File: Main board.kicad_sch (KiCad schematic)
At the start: 101 parts, among them CN1 PA001-4P, CN2 PA001-4P, J1 Conn_ARM_SWD_TagConnect_TC203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, J2 Conn_01x03_Pin, J3 Conn_01x03_Pin, J5 Connector, USB-TYPE-C-16P, J6 436500201, J7 Conn_01x04_Pin, J8 Conn_01x04_Pin, Q1 SI7232DN-T1-GE3, Q2 SI7232DN-T1-GE3, SW1 SKRKAEE020, SW2 SKRKAEE020, U1 STM32U575VGTx, U10 TLV75733PDBV, U11 NRVB120VLSFT1G, U12 NRVB120VLSFT1G, U2 TPS62901RPJR, U7 SN74AHCT125DR, X1 1XXD32000MBA, Y1 ECS-327TXO-33-TR

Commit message: fix and back to basic
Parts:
- removed CN1, CN2: PA001-4P, EASYEDA:CONN-TH_4P-P5.08_PA001-4P, symbol EasyEDA:PA001-4P
- removed J2, J3: Conn_01x03_Pin, Connector_PinHeader_2.54mm:PinHeader_1x03_P2.54mm_Horizontal, symbol Connector:Conn_01x03_Pin
- added CN1, CN2: PA001-6P, Mainboard_local:CONN-TH_6P-P5.00_PA001-6P, symbol Mainboard_local:PA001-6P
- added J2: Conn_01x02_Pin, Connector_PinHeader_2.54mm:PinHeader_1x02_P2.54mm_Vertical, symbol Connector:Conn_01x02_Pin
- added J3: Conn_01x02_Pin, Connector_AMASS:AMASS_XT30PW-F_1x02_P2.50mm_Horizontal, symbol Connector:Conn_01x02_Pin
- added SW3, SW4: SW_SPDT, EasyEDA:SW-TH_3P-L8.8-W3.9-P2.50_SS12D00G3, symbol Switch:SW_SPDT
- C1, C25, C26, C35, C36: footprint PCM_JLCPCB:C_0603 -> PCM_JLCPCB:C_0402; LCSC C96446 -> C15525; Price 0.007USD -> 0.009USD; Stock 2048985 -> 3940889; Voltage Rated 25V -> 6.3V
- C10, C11, C12, C15, C2, C3, C30, C4, C5, C6, C7, C8, C9: Stock 12931403 -> 20208285
- C13, C14: Stock 4952869 -> 7021828
- C27, C31: Price 0.017USD -> 0.021USD; Stock 2472302 -> 3388297
- C28: footprint PCM_JLCPCB:C_0805 -> PCM_JLCPCB:C_0603; LCSC C380338 -> C59461; Price 0.010USD -> 0.012USD; Stock 1921885 -> 5081183; Voltage Rated 10V -> 6.3V
- C29: Stock 2965057 -> 4779042
- C32, C37: Stock 52215439 -> 70324515
- C34: footprint PCM_JLCPCB:C_0805 -> PCM_JLCPCB:C_0402; LCSC C76639 -> C23733; Stock 1920914 -> 4366811
- J7: value Conn_01x04_Pin -> Conn_01x02_Pin; footprint Connector_JST:JST_XH_B4B-XH-A_1x04_P2.50mm_Vertical -> Connector_JST:JST_XH_B2B-XH-A_1x02_P2.50mm_Vertical; symbol Connector:Conn_01x04_Pin -> Connector:Conn_01x02_Pin
- R1, R10, R11, R12, R13, R19, R9: Attrition Qty 0 -> 10; LCSC C25744 (OUT OF STOCK) -> C25744; Minimum Qty 5 -> 20; Stock 10588972 -> 24372091
- R15, R16, R3, R4: Stock 1915978 -> 7466061
- R2, R32, R33, R34: Stock 858002 -> 967219
- R20: Stock 4940693 -> 5907585
- R21, R29, R39, R44: Stock 591787 -> 1007760
- R22, R23: Stock 2252456 -> 3534773
- R24: LCSC - -> C22764; Manufacturer Panasonic -> UNI-ROYAL(Uniroyal Elec); Part ERJ-P03F7682V -> 0603WAF1101T5E; Power(Watts) 200mW -> 100mW; Resistance 76.8kΩ -> 1.1kΩ; Stock 71476 -> 156127
- R25: LCSC - -> C22764; Manufacturer Panasonic -> UNI-ROYAL(Uniroyal Elec); Part ERJ-S03F2612V -> 0603WAF1101T5E; Resistance 26.1kΩ -> 1.1kΩ; Stock 71476 -> 156127
- R26: Stock 28829731 -> 51181774
- R27: Stock 1745486 -> 1792808
- R28: Stock 230104 -> 203255
- R35, R36, R37, R38: Stock 8207005 -> 13226393
- R40, R41, R42, R43: Stock 663196 -> 859014
- R5, R8: Stock 480893 -> 771013
- R7: LCSC C25741 (OUT OF STOCK) -> C25741; Stock 4653113 -> 6969783
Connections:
- net GNDA is gone; now on net GND: H1.1, H2.1, H3.1, H4.1
- net +3V3: no longer J7.1 (Pin_1)
- net GND: now also CN1.4, CN2.4, J2.2 (Pin_2), J3.2 (Pin_2); no longer J7.2 (Pin_2)
- net PYRO+: now also CN1.1, CN2.1, SW3.3 (C), SW4.3 (C)
- net SERVO1: now also CN1.5
- net SERVO2: now also CN2.5
- net USART1_RX: now also J7.2 (Pin_2); no longer J7.4 (Pin_4)
- net USART1_TX: now also J7.1 (Pin_1); no longer J7.3 (Pin_3)
- net VBAT+: now also J3.1 (Pin_1)
- net at Q1.5 (D2), Q1.6 (D2), R41.2: now also CN1.6
- net at Q1.7 (D1), Q1.8 (D1), R40.2: now also CN1.2
- net at Q2.5 (D2), Q2.6 (D2), R42.2: now also CN2.6
- net at Q2.7 (D1), Q2.8 (D1), R43.2: now also CN2.2
- new net: CN2.3, SW4.2 (B)
- new net: CN1.3, SW3.2 (B)
- new net BEC+: J2.1 (Pin_1), SW3.1 (A), SW4.1 (A)
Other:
- note added: "A0 · Mounting Holes"
- note added: "A1 · Battery Input & Protection"
- note added: "A1.2 · Battery Voltage Sense (ADC divider)"
- note added: "A2 · 5V Buck (TPS62901RPJR set for vset mode)"
- note added: "A3 · 3.3V LDO (TLV75733)"
- note added: "A4 · BEC interface (servo supply rail)"
- note added: "A5 · Actuation"
- note added: "B1 · MCU Core - STM32U575"
- note added: "B1 · MCU Decoupling"
- note added: "B2 · Clock - 32 MHz HSE (X1)"
- note added: "B2 · Clock - 32.768 kHz LSE (Y1)"
- note added: "B4 · microSD Storage"
- note added: "B5 · Actuation - Servo Level Shift"
- note added: "C1 · USB Interface + ESD diodes"
- note added: "C2 · Comms - USART1 (Companion)"
- note added: "C2 · Comms - USART3 (Telemetry)"
- note added: "D1 · BOOT0 Button"
- note added: "D1 · Reset Button"
- note added: "D1 · Status LEDs"
- note added: "D2 · SWD Debug (TagConnect)"
- note removed: "3.3V LDO"
- note removed: "5V Buck (TPS62901RPJR set for vset mode)"
- note removed: "BOOT0 switch"
- note removed: "Battery Connector"
- note removed: "Companion USART1"
- note removed: "Debugging"
- note removed: "Divider circuit for ADC"
- note removed: "LSE 32.7680 kHz"
- note removed: "MCU Power and Decoupling"
- note removed: "Manual reset"
- note removed: "PWM Level Shifting"
- note removed: "Pyrotechnique channels"
- note removed: "SD Card slot"
- note removed: "STM32U5"
- note removed: "TCXO"
- note removed: "Transmission USART3"
- note removed: "USB + ESD diodes"
- company: Chulalongkorn University High Altitude Research (CUHAR) -> (none)
- title: CURFA-V SRAD Flight Computer -> CANSR-I SRAD Flight Computer
- moved on the sheet: C1, C10, C11, C12, C13, C14, C15, C2, C25, C26, C27, C28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

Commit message: fix + start leyout
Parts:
- C30, D2, R27, R28: now left out of the parts list
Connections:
- net BEC+: now also J2.2 (Pin_2); no longer J2.1 (Pin_1)
- net GND: now also J2.1 (Pin_1), J3.1 (Pin_1), J6.1; no longer J2.2 (Pin_2), J3.2 (Pin_2), J6.2
- net PYRO+: now also J6.2; no longer J6.1
- net VBAT+: now also J3.2 (Pin_2); no longer J3.1 (Pin_1)
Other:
- moved on the sheet: C31, C32, D3, J3, J6, JP1

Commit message: Update Main board.kicad_sch
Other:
- title: CANSR-I SRAD Flight Computer -> COMSR-I
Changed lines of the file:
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@@
 	(paper "A3")
 	(title_block
-		(title "CANSR-I SRAD Flight Computer")
+		(title "COMSR-I")
 		(rev "1.1.31")
 	)

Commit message: koiiin
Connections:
- net at SW4.2 (B): now also CN2.6; no longer CN2.3
- net at SW3.2 (B): now also CN1.6; no longer CN1.3
- net at Q1.5 (D2), Q1.6 (D2), R41.2: now also CN1.3; no longer CN1.6
- net at Q2.5 (D2), Q2.6 (D2), R42.2: now also CN2.3; no longer CN2.6
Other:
- moved on the sheet: CN1, CN2

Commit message: 80%layout
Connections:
- net FIRE_C: now also U1.7 (PC13); no longer U1.9 (PC15)
- net FIRE_D: now also U1.9 (PC15); no longer U1.7 (PC13)
- net PWM1: now also U7.5 (2A); no longer U7.2 (1A)
- net PWM2: now also U7.2 (1A); no longer U7.5 (2A)
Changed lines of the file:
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@@
 	(wire
 		(pts
+			(xy 273.05 165.1) (xy 274.32 165.1)
+		)
+		(stroke
+			(width 0)
+			(type default)
+		)
+	)
+	(wire
+		(pts
 			(xy 153.67 229.87) (xy 148.59 229.87)
 		)
@@
 	(wire
 		(pts
+			(xy 273.05 170.18) (xy 274.32 170.18)
+		)
+		(stroke
+			(width 0)
+			(type default)
+		)
+	)
+	(wire
+		(pts
 			(xy 19.05 36.83) (xy 26.67 36.83)
 		)
@@
 	(wire
 		(pts
+			(xy 120.65 125.73) (xy 128.27 125.73)
+		)
+		(stroke
+			(width 0)
+			(type default)
+		)
+	)
+	(wire
+		(pts
 			(xy 273.05 99.06) (xy 274.32 99.06)
 		)
@@
 	(wire
 		(pts
-			(xy 339.09 86.36) (xy 349.25 86.36)
+			(xy 120.65 133.35) (xy 128.27 133.35)
 		)
 		(stroke
@@
 	(wire
 		(pts
-			(xy 40.64 139.7) (xy 59.69 139.7)
+			(xy 339.09 86.36) (xy 349.25 86.36)
 		)
 		(stroke
@@
 	(wire
 		(pts
-			(xy 44.45 182.88) (xy 46.99 182.88)
+			(xy 40.64 139.7) (xy 59.69 139.7)
 		)
 		(stroke
@@
 	(wire
 		(pts
-			(xy 252.73 33.02) (xy 255.27 33.02)
+			(xy 44.45 182.88) (xy 46.99 182.88)
 		)
 		(stroke
@@
 	(wire
 		(pts
-			(xy 40.64 129.54) (xy 49.53 129.54)
+			(xy 252.73 33.02) (xy 255.27 33.02)
 		)
 		(stroke
@@
 	(wire
 		(pts
-			(xy 45.72 36.83) (xy 26.67 36.83)
+			(xy 40.64 129.54) (xy 49.53 129.54)
 		)
 		(stroke
@@
 	(wire
 		(pts
-			(xy 26.67 39.37) (xy 36.83 39.37)
+			(xy 45.72 36.83) (xy 26.67 36.83)
 		)
 		(stroke
@@
 	(wire
 		(pts
-			(xy 116.84 125.73) (xy 128.27 125.73)
+			(xy 26.67 39.37) (xy 36.83 39.37)
 		)
 		(stroke
@@
 	(wire
 		(pts
-			(xy 116.84 133.35) (xy 128.27 133.35)
-		)
-		(stroke
-			(width 0)
-			(type default)
-		)
-	)
-	(wire
-		(pts
 			(xy 330.2 113.03) (xy 330.2 111.76)
 		)
@@
 	(global_label "FIRE_D"
 		(shape output)
-		(at 273.05 165.1 0)
+		(at 274.32 170.18 0)
 		(fields_autoplaced yes)
 		(effects
@@
 		)
 		(property "Intersheetrefs" "${INTERSHEET_REFS}"
-			(at 282.3852 165.1 0)
+			(at 283.6552 170.18 0)
 			(effects
 				(font
@@
 	(global_label "PWM2"
 		(shape input)
-		(at 116.84 133.35 180)
+		(at 120.65 125.73 180)
 		(fields_autoplaced yes)
 		(effects
@@
 		)
 		(property "Intersheetrefs" "${INTERSHEET_REFS}"
-			(at 108.4725 133.35 0)
+			(at 112.2825 125.73 0)
 			(effects
 				(font
@@
 	(global_label "PWM1"
 		(shape input)
-		(at 116.84 125.73 180)
+		(at 120.65 133.35 180)
 		(fields_autoplaced yes)
 		(effects
@@
 		)
 		(property "Intersheetrefs" "${INTERSHEET_REFS}"
-			(at 108.4725 125.73 0)
+			(at 112.2825 133.35 0)
 			(effects
 				(font
@@
 	(global_label "FIRE_C"
 		(shape output)
-		(at 273.05 170.18 0)
+		(at 274.32 165.1 0)
 		(fields_autoplaced yes)
 		(effects
@@
 		)
 		(property "Intersheetrefs" "${INTERSHEET_REFS}"
-			(at 282.3852 170.18 0)
+			(at 283.6552 165.1 0)
 			(effects
 				(font
@@
 		)
 		(property "Digikey Part No." "311-10.0KLRCT-ND"
-			(at 392.43 41.91 0)
+			(at 388.62 39.878 0)
 			(effects
 				(font
@@
 		)
 		(property "Digikey Part No." "311-10.0KLRCT-ND"
-			(at 392.43 48.26 0)
+			(at 409.448 48.768 0)
 			(effects
 				(font
@@
 		)
 		(property "Digikey Part No." "311-10.0KLRCT-ND"
-			(at 392.43 34.29 0)
+			(at 404.622 34.29 0)
 			(effects
 				(font
@@
 		(dnp no)
 		(property "Reference" "R9"
-			(at 392.43 24.765 90)
+			(at 391.922 25.146 90)
 			(effects
 				(font
@@
 		)
 		(property "Digikey Part No." "311-10.0KLRCT-ND"
-			(at 392.43 27.94 0)
+			(at 376.936 28.448 0)
 			(effects
 				(font
@@
 		)
 		(property "Digikey Part No." "311-10.0KLRCT-ND"
-			(at 392.43 54.61 0)
+			(at 402.082 57.15 0)
 			(effects
 				(font

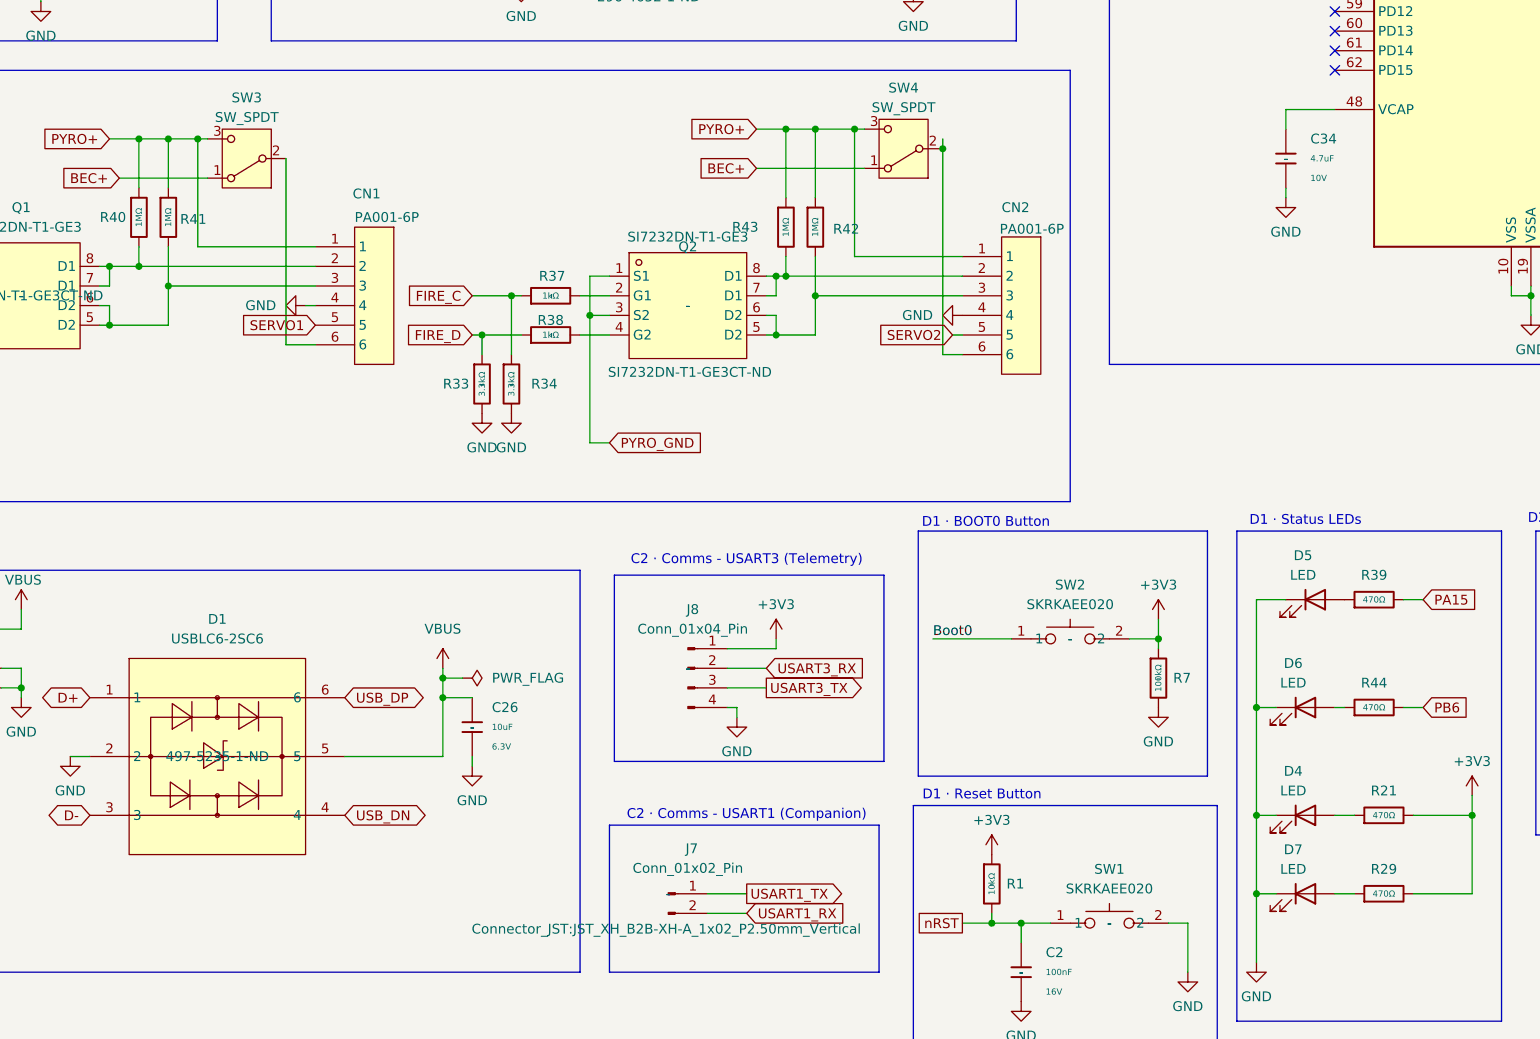
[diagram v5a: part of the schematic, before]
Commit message: add LED for Barometer and IMU
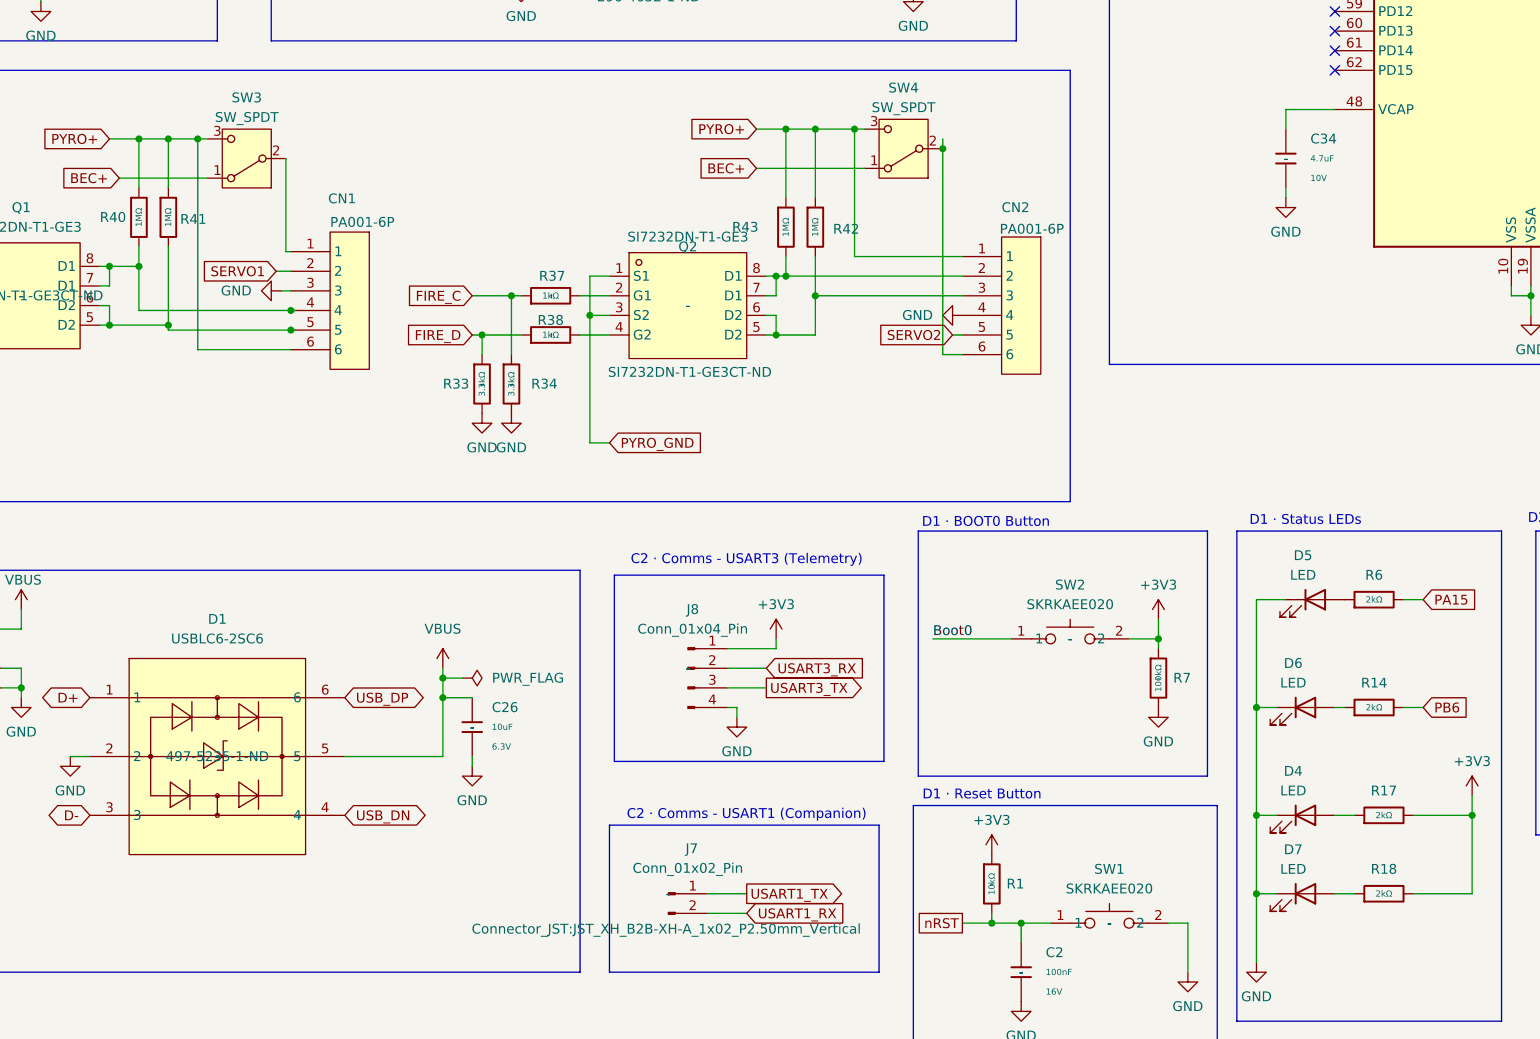
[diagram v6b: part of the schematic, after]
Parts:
- removed R21, R29, R39, R44: 470Ω, PCM_JLCPCB:R_0402, symbol PCM_JLCPCB-Resistors:0402,470Ω
- added R14, R17, R18, R6: 2kΩ, PCM_JLCPCB:R_0402, symbol PCM_JLCPCB-Resistors:0402,2kΩ
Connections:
- net +3V3: now also R17.2, R18.2
- net GND: now also CN1.3; no longer CN1.4
- net PA15: now also R6.2
- net PB6: now also R14.2
- net PYRO+: now also CN1.6; no longer CN1.1
- net SERVO1: now also CN1.2; no longer CN1.5
- net at SW3.2 (B): now also CN1.1; no longer CN1.6
- net at Q1.5 (D2), Q1.6 (D2), R41.2: now also CN1.5; no longer CN1.3
- net at Q1.7 (D1), Q1.8 (D1), R40.2: now also CN1.4; no longer CN1.2
- net at D7.2 (A): now also R18.1
- net at D4.2 (A): now also R17.1
- net at D5.2 (A): now also R6.1
- net at D6.2 (A): now also R14.1
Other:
- moved on the sheet: CN1
